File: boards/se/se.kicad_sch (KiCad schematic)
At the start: 34 parts, among them J3 Conn_02x05_Odd_Even, U1 ENC624J600-PT, U3 GAL16V8, U5 LD1117S33TR_SOT223, Y1 25MHz

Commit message: Rev1 hardware
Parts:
- removed U3: GAL16V8, Package_LCC:PLCC-20_THT-Socket, symbol Logic_Programmable:GAL16V8
- added C13 (x4): 1uF, Capacitor_SMD:C_0805_2012Metric_Pad1.18x1.45mm_HandSolder, symbol Device:C
- added J3: Conn_01x07, Connector_PinHeader_2.54mm:PinHeader_1x07_P2.54mm_Vertical, symbol Connector_Generic:Conn_01x07
- added U2: ATF1502AS-xAx44, Package_QFP:TQFP-44_10x10mm_P0.8mm, symbol CPLD_Microchip:ATF1502AS-xAx44
- added U3: 74LVC2G17, Package_TO_SOT_SMD:SOT-363_SC-70-6, symbol 74xGxx:74LVC2G17
- C1: renamed from C16; footprint Capacitor_SMD:C_0805_2012Metric_Pad1.18x1.45mm_HandSolder -> Capacitor_SMD:C_1206_3216Metric_Pad1.33x1.80mm_HandSolder; Digikey C0805X102K102T -> 4587-C1206X102K202TCT-ND; LCSC (none) -> C282813
- C10, C7, C8, C9: Digikey C0805C104M5RAC7800 -> 399-C0805C104M5RAC7800CT-ND; LCSC (none) -> C49678
- C11, C13: Digikey CL21B105KAFNNNE -> 1276-1066-1-ND; LCSC (none) -> C28323
- C18: renamed from C9; Digikey 293D106X0010A2TE3 -> 718-1118-1-ND; LCSC (none) -> C7171
- C2: renamed from C15; Digikey C0805C103K5RAC7800 -> 399-C0805C103K5RACTUCT-ND; LCSC (none) -> C1710
- C21: renamed from C18; Digikey 293D106X0010A2TE3 -> 718-1118-1-ND; LCSC (none) -> C7171
- C22: renamed from C17; Digikey C0805C104M5RAC7800 -> 399-C0805C104M5RAC7800CT-ND; LCSC (none) -> C49678
- C3: renamed from C14; Digikey C0805C103K5RAC7800 -> 399-C0805C103K5RACTUCT-ND; LCSC (none) -> C1710
- C4: renamed from C13; Digikey C0805C682K5RAC7800 -> 399-C0805C682K5RAC7800CT-ND; LCSC (none) -> C1755
- C5: renamed from C12; Digikey C0805C682K5RAC7800 -> 399-C0805C682K5RAC7800CT-ND; LCSC (none) -> C1755
- C5, C6: Digikey C0805C180K5GAC7800 -> 399-C0805C180K5GAC7800CT-ND; LCSC (none) -> C1797
- FB1: Digikey BBPY00201209331Y00 -> 240-2549-1-ND; LCSC (none) -> C1015
- J3: Digikey 302-S101 -> 2057-BHR-08-HUA-ND; LCSC (none) -> C2843202
- R1: renamed from R10; Digikey RMCF0805FT75R0 -> RMCF0805FT75R0CT-ND; LCSC (none) -> C2933566
- R2: renamed from R11; Digikey RMCF0805FT75R0 -> RMCF0805FT75R0CT-ND; LCSC (none) -> C2933566
- R3: renamed from R7; Digikey RMCF0805FT10R0 -> RMCF0805FT10R0CT-ND; LCSC (none) -> C17415
- R4: renamed from R9; Digikey RMCF0805FT49R9 -> RMCF0805FT49R9CT-ND; LCSC (none) -> C17720
- R5: renamed from R8; Digikey RMCF0805FT49R9 -> RMCF0805FT49R9CT-ND; LCSC (none) -> C17720
- R6: Digikey RMCF0805FT49R9 -> RMCF0805FT49R9CT-ND; LCSC (none) -> C17720
- R7: renamed from R4; Digikey RMCF0805FT49R9 -> RMCF0805FT49R9CT-ND; LCSC (none) -> C17720
- R8: renamed from R1; Digikey RMCF0805FT12K4 -> RMCF0805FT12K4CT-ND; LCSC (none) -> C317429
- R9: renamed from R5; Digikey RMCF0805FT10K0 -> RMCF0805FT10K0CT-ND; LCSC (none) -> C17414
- TR1: Digikey PT61018PEL -> PT61018PELCT-ND; LCSC (none) -> C510548
- U1: Digikey ENC624J600-I/PT -> ENC624J600-I/PT-ND; LCSC (none) -> C630732
- U4: renamed from U5; Digikey LD1117S33TR -> 497-1242-1-ND; LCSC (none) -> C6186
- Y1: Digikey 2151-RH100-25.000-18-F-1020-EXT-TRDKR-ND -> 2151-RH100-25.000-18-F-1020-EXT-TRCT-ND; LCSC (none) -> C9006
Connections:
- net +3.3V: no longer R9.1
- net +5V: now also C13.1, C13.1, C13.1, C13.1, J3.5 (Pin_5), U2.17 (VCC), U2.29 (VCC), U2.41 (VCC), U2.9 (VCC), U3.5 (VCC)
- net A16: now also U2.22 (I/O)
- net A17: now also U2.21 (I/O)
- net A18: now also U2.20 (I/O)
- net A19: now also U2.19 (I/O/PD2)
- net A20: now also U2.18 (I/O)
- net A21: now also U2.15 (I/O)
- net A22: now also U2.14 (I/O)
- net A23: now also U2.13 (I/O)
- net B0SEL: now also U2.2 (I/O), U3.3; no longer U1.50 (WR/WRL/B0SEL/SO)
- net B1SEL: now also U2.3 (I/O), U3.1; no longer U1.48 (WRH/B1SEL)
- net ETH_~{INT}: now also U2.6 (I/O)
- net GND: now also R9.1, C13.2, C13.2, C13.2, C13.2, J3.6 (Pin_6), U2.16 (GND), U2.24 (GND), U2.36 (GND), U2.4 (GND), U3.2 (GND)
- net R/~{W}: now also U2.31 (I/O)
- net ~{AS}: now also U2.25 (I/O)
- net ~{IPL0}: now also U2.10 (I/O)
- net ~{IPL1}: now also U2.11 (I/O)
- net ~{LDS}: now also U2.28 (I/O)
- net ~{UDS}: now also U2.27 (I/O)
- net ETH_CS: now reaches U1.49 (~{CS}/CS)
- net ETH_CS: now also U2.5 (I/O/PD1)
- net ETH_CLK: now reaches U1.33 (CLKOUT)
- net ETH_CLK: now also U2.8 (I/O)
- new net B0SEL': U1.50 (WR/WRL/B0SEL/SO), U3.4
- new net B1SEL': U1.48 (WRH/B1SEL), U3.6
- new net CPLD_VPP: J3.7 (Pin_7), U2.38 (I/OE1/Vpp)
- new net TCK: J3.2 (Pin_2), U2.26 (I/O/TCK)
- new net TDI: J3.3 (Pin_3), U2.1 (I/O/TDI)
- new net TDO: J3.4 (Pin_4), U2.32 (I/O/TDO)
- new net TMS: J3.1 (Pin_1), U2.7 (I/O/TMS)
- new net ~{DTACK}: U2.30 (I/O)
- new net ~{EXT_DTK}: U2.12 (I/O)
- new net ~{RESET}: U2.23 (I/O)
- no-connect marks 2 -> 9
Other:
- moved on the sheet: C10, C13, C21, C22, C7, C8, C9, FB1, J3, R9, U4

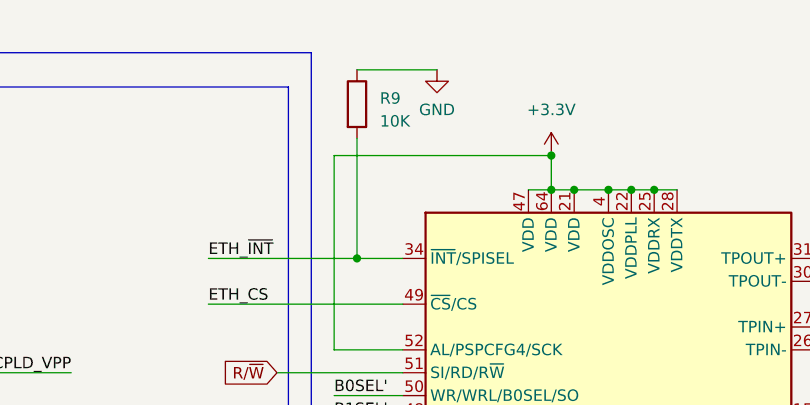
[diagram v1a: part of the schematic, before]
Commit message: SPISEL pulldown resistor should be 100K, not 10K
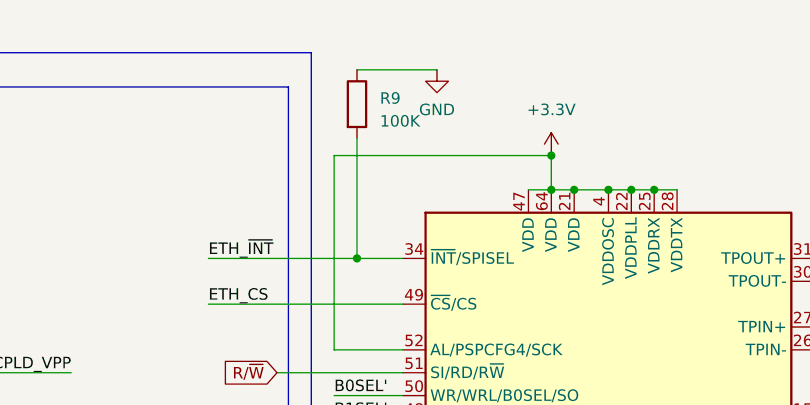
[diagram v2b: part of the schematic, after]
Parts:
- R9: value 10K -> 100K; Digikey RMCF0805FT10K0CT-ND -> (none); LCSC C17414 -> (none)
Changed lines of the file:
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@@
       (effects (font (size 1.27 1.27)) (justify left))
     )
-    (property "Value" "10K" (at 115.57 24.13 0)
+    (property "Value" "100K" (at 115.57 24.13 0)
       (effects (font (size 1.27 1.27)) (justify left))
     )
@@
       (effects (font (size 1.27 1.27)) hide)
     )
-    (property "Digikey" "RMCF0805FT10K0CT-ND" (at 113.03 22.225 0)
+    (property "Digikey" "" (at 113.03 22.225 0)
       (effects (font (size 1.27 1.27)) hide)
     )
-    (property "LCSC" "C17414" (at 113.03 22.225 0)
+    (property "LCSC" "" (at 113.03 22.225 0)
       (effects (font (size 1.27 1.27)) hide)
     )

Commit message: update schematics
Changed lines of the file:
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@@
     (effects (font (size 1.27 1.27)) (justify left top))
   )
-  (text_box "The ENC624J600 requires a 1ns delay between asserting CS and asserting B0SEL/B1SEL. The propagation delay of a 74LVC2G17 buffer is perfect for this."
-    (at 31.75 144.78 0) (size 44.45 10.16)
+  (text_box "The ENC624J600 requires a 1ns delay between asserting CS and asserting B0SEL/B1SEL. U3 was placed to provide a small propagation delay for this, but it was insufficient, and a feedback path through the CPLD was found to be preferable."
+    (at 31.75 140.97 0) (size 44.45 13.97)
     (stroke (width -0.0001) (type default))
     (fill (type none))
